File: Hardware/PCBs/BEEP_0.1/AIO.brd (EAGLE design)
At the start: 102 x 102 mm, 89 parts, among them U1 ATXMEGA64D3-AU, U2 TB6612FNG

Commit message: enhance robot case enhance main circuit
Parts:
- removed JP10: (no value), pinhead:1X08
- removed U$10, U$11, U$12, U$14, U$15, U$16, U$17, U$18, U$19, U$20, U$6, U$7, U$8, U$9: DMN2075U, BEEP:SOT95P240X112-3N
- added IC1, IC2: ULN2803ASOP18, BEEP:SOP18
- added JP12: Step_Down_Conn, pinhead:1X03
- added JP13: batt_conn, pinhead:1X02
- added LED11: (no value), led:CHIPLED_0603
- added R35, R36, R37, R38, R40, R41: 100R, rcl:R0402
- added R39: 47K, rcl:R0402
- added R42: (no value), rcl:R0402
- added S1, S2: (no value), switch-omron:B3F-31XX
- JP11: value (none) -> Color_Conn
- JP9: value (none) -> Motor_Conn; device pinhead:1X08 -> pinhead:1X04
- R34: value (none) -> 10K
- moved R34 132.4 mm to (40.6, 66.0)
- moved C5 81.2 mm to (14.0, 47.0)
- moved LED10 81.2 mm to (14.0, 55.9)
- moved LED9 81.2 mm to (19.1, 55.9)
- moved R28 81.2 mm to (24.1, 62.2)
- moved R29 81.2 mm to (24.1, 58.4)
- moved R30 81.2 mm to (24.1, 54.6)
- moved R33 81.2 mm to (14.0, 38.1)
- moved R31 81.2 mm to (14.0, 50.8)
- moved R32 81.2 mm to (14.0, 41.9)
- moved JP8 79.5 mm to (100.3, 0.00), turned to 225 degrees
- moved U$5 71.9 mm to (15.2, 47.0), turned to 0 degrees
- moved R5 49.9 mm to (97.8, 68.6)
- moved JP11 48.1 mm to (10.2, 41.9), turned to 90 degrees
- moved JP5 38.2 mm to (11.4, 3.81)
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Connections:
- removed net IR_DISTANCE_0: U$12.G
- removed net IR_DISTANCE_1: U$14.G
- removed net IR_DISTANCE_2: U$15.G
- removed net IR_DISTANCE_3: U$16.G
- removed net IR_DISTANCE_4: U$17.G
- removed net IR_DISTANCE_5: U$18.G
- removed net IR_DISTANCE_6: U$19.G
- removed net IR_DISTANCE_7: U$20.G
- removed net LEDA1: U$3.G
- removed net LEDA2: U$2.G
- removed net LEDA3: U$1.G
- removed net LEDK1: U$4.G
- removed net LEDK2: U$5.G
- removed net LEDK3: U$6.G
- removed net LEDK4: U$7.G
- removed net LEDK5: U$8.G
- removed net LEDK6: U$9.G
- removed net LEDK7: U$10.G
- removed net LEDK8: U$11.G
- removed net N$28: R14.1, U$18.S
- removed net N$31: R16.1, U$19.S
- removed net N$37: R18.1, U$20.S
- new net BATT_GND: JP13.2, U$5.S
- new net IR_LED1: IC2.1
- new net IR_LED2: IC2.2
- new net IR_LED3: IC2.3
- new net IR_LED4: IC2.4
- new net IR_LED5: IC2.5
- new net IR_LED6: IC2.6
- new net IR_LED7: IC2.7
- new net IR_LED8: IC2.8
- new net IR_PWM: R40.1
- new net LED1: IC1.1
- new net LED2: IC1.2
- new net LED3: IC1.3
- new net LED4: IC1.4
- new net LED5: IC1.5
- new net LED6: IC1.6
- new net LED7: IC1.7
- new net LED8: IC1.8
- new net LED_A1: R35.1
- new net LED_A2: R36.1
- new net LED_A3: R37.1
- new net N$38: R35.2, U$3.G
- new net N$39: R36.2, U$2.G
- new net N$40: R37.2, U$1.G
- new net N$41: U$26.5V@1, U$26.5V@2, U$4.S
- new net N$42: R38.2, R39.1, U$4.G
- new net N$43: IC2.15, JP4.3
- new net N$44: IC2.18, JP1.3
- new net N$45: IC2.17, JP2.3
- new net N$46: IC2.16, JP3.3
- new net N$47: IC2.13, JP6.3
- new net N$48: IC2.14, JP5.3
- new net N$49: IC2.12, JP7.3
- new net RPI_IKILL: R38.1
- net +3V3: no longer JP10.7
- net +5V: now also JP12.3, R39.2, U$13.D, U$4.D; no longer U$12.D, U$14.D, U$15.D, U$16.D, U$17.D, U$18.D, U$19.D, U$20.D, U$26.5V@1, U$26.5V@2
- net +7V: now also JP12.1, JP13.1, LED11.A, R41.1; no longer JP10.8
- net GND: now also IC1.9, IC2.9, JP12.2, R42.2, S1.2, S2.2, U$5.D; no longer JP10.1, JP10.6, JP9.8, U$10.S, U$11.S, U$13.S, U$4.S, U$5.S, U$6.S, U$7.S, U$8.S, U$9.S
- net IR_LED_PWM: now also R40.2
- net MOTOR_A_IN1: no longer JP9.3
- net MOTOR_A_IN2: no longer JP9.2
- net MOTOR_A_OUT1: now also JP9.4; no longer JP10.5
- net MOTOR_A_OUT2: now also JP9.3; no longer JP10.4
- net MOTOR_A_PWM: no longer JP9.1
- net MOTOR_B_IN1: no longer JP9.5
- net MOTOR_B_IN2: no longer JP9.6
- net MOTOR_B_OUT1: now also JP9.1; no longer JP10.2
- net MOTOR_B_OUT2: now also JP9.2; no longer JP10.3
- net MOTOR_B_PWM: no longer JP9.7
- net MOTOR_STBY: no longer JP9.4
- net N$10: now also IC1.15; no longer U$7.D
- net N$12: now also R10.1, R12.1, R14.1, R16.1, R18.1, R4.1, R8.1, U$13.S; no longer U$14.S
- net N$13: now also IC2.11; no longer JP1.3, JP2.3, JP3.3, JP4.3, JP5.3, JP6.3, JP7.3, U$13.D
- net N$14: now also IC1.14; no longer U$8.D
- net N$15: now also IC1.13; no longer U$9.D
- net N$16: now also IC1.12; no longer U$10.D
- net N$17: now also IC1.11; no longer U$11.D
- net N$19: now also LED11.C, R42.1; no longer R8.1, U$15.S
- net N$22: now also S1.1, U$26.GPIO_23; no longer R10.1, U$16.S
- net N$25: now also S2.1, U$26.GPIO_22; no longer R12.1, U$17.S
- net N$4: now also IC1.17; no longer U$5.D
- net N$6: now also IC1.18; no longer U$4.D
- net N$7: now also IC1.16; no longer U$6.D
- net N$8: now also R41.2, U$5.G; no longer R4.1, U$12.S
- net SCL: now also U$26.GPIO_1
- net SDA: now also U$26.GPIO_0
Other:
- board size 102 x 102 mm -> 105 x 80 mm

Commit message: minor enhancement of robot case enhancements of RPi Footprint enhance main pcb add pcb space drawing
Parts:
- moved IC2 18.0 mm to (50.8, 34.3), turned to 90 degrees
- moved U1 11.5 mm to (67.3, 39.4)
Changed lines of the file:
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@@
 </autorouter>
 <elements>
-<element name="U1" library="atmel-xmega" package="TQFP-64A-64" value="ATXMEGA64D3-AU" x="78.74" y="38.1"/>
+<element name="U1" library="atmel-xmega" package="TQFP-64A-64" value="ATXMEGA64D3-AU" x="67.31" y="39.37"/>
 <element name="LED1" library="BEEP" package="5050LED" value="F503605050" x="25.4" y="72.39"/>
 <element name="LED2" library="BEEP" package="5050LED" value="F503605050" x="74.93" y="8.89" rot="R180"/>
@@
 <element name="R38" library="rcl" package="R0402" value="100R" x="40.64" y="34.29"/>
 <element name="R39" library="rcl" package="R0402" value="47K" x="40.64" y="30.48"/>
-<element name="IC2" library="BEEP" package="SOP18" value="ULN2803ASOP18" x="63.5" y="21.59"/>
+<element name="IC2" library="BEEP" package="SOP18" value="ULN2803ASOP18" x="50.8" y="34.29" rot="R90"/>
 <element name="R40" library="rcl" package="R0402" value="100R" x="12.7" y="55.88"/>
 <element name="U$5" library="BEEP" package="SOT95P240X112-3N" value="DMN2075U" x="15.24" y="46.99"/>
@@
 <wire x1="56.205" y1="55.726" x2="57.505" y2="48.414" width="0" layer="19" extent="1-1"/>
 <wire x1="13.32" y1="67.31" x2="24.78" y2="58.42" width="0" layer="19" extent="1-1"/>
-<wire x1="75.94" y1="45.9" x2="58.155" y2="48.414" width="0" layer="19" extent="1-1"/>
-<wire x1="82.34" y1="45.9" x2="75.94" y2="45.9" width="0" layer="19" extent="1-1"/>
-<wire x1="83.17" y1="41.91" x2="82.34" y2="45.9" width="0" layer="19" extent="1-1"/>
-<wire x1="86.54" y1="40.9" x2="83.17" y2="41.91" width="0" layer="19" extent="1-1"/>
-<wire x1="86.54" y1="32.9" x2="86.54" y2="40.9" width="0" layer="19" extent="1-1"/>
-<wire x1="78.34" y1="30.3" x2="86.54" y2="32.9" width="0" layer="19" extent="1-1"/>
-<wire x1="73.66" y1="26.065" x2="78.34" y2="30.3" width="0" layer="19" extent="1-1"/>
-<wire x1="70.94" y1="33.7" x2="73.66" y2="26.065" width="0" layer="19" extent="1-1"/>
-<wire x1="68.58" y1="17.115" x2="73.66" y2="26.065" width="0" layer="19" extent="1-1"/>
-<wire x1="66.69" y1="11.43" x2="68.58" y2="17.115" width="0" layer="19" extent="1-1"/>
+<wire x1="64.51" y1="47.17" x2="58.155" y2="48.414" width="0" layer="19" extent="1-1"/>
+<wire x1="70.91" y1="47.17" x2="64.51" y2="47.17" width="0" layer="19" extent="1-1"/>
+<wire x1="83.17" y1="41.91" x2="70.91" y2="47.17" width="0" layer="19" extent="1-1"/>
+<wire x1="75.11" y1="42.17" x2="83.17" y2="41.91" width="0" layer="19" extent="1-1"/>
+<wire x1="75.11" y1="34.17" x2="75.11" y2="42.17" width="0" layer="19" extent="1-1"/>
+<wire x1="66.91" y1="31.57" x2="75.11" y2="34.17" width="0" layer="19" extent="1-1"/>
+<wire x1="73.66" y1="26.065" x2="66.91" y2="31.57" width="0" layer="19" extent="1-1"/>
+<wire x1="59.51" y1="34.97" x2="73.66" y2="26.065" width="0" layer="19" extent="1-1"/>
+<wire x1="55.275" y1="39.37" x2="73.66" y2="26.065" width="0" layer="19" extent="1-1"/>
+<wire x1="66.69" y1="11.43" x2="55.275" y2="39.37" width="0" layer="19" extent="1-1"/>
 <wire x1="63.5" y1="5.89" x2="66.69" y2="11.43" width="0" layer="19" extent="1-1"/>
-<wire x1="79.36" y1="11.43" x2="68.58" y2="17.115" width="0" layer="19" extent="1-1"/>
-<wire x1="99.0346" y1="44.1706" x2="86.54" y2="40.9" width="0" layer="19" extent="1-1"/>
+<wire x1="79.36" y1="11.43" x2="55.275" y2="39.37" width="0" layer="19" extent="1-1"/>
+<wire x1="99.0346" y1="44.1706" x2="75.11" y2="42.17" width="0" layer="19" extent="1-1"/>
 </signal>
 <signal name="N$10">
@@
 <contactref element="JP6" pad="2"/>
 <wire x1="96.52" y1="60.96" x2="86.36" y2="73.66" width="0" layer="19" extent="1-1"/>
-<wire x1="81.54" y1="45.9" x2="96.52" y2="60.96" width="0" layer="19" extent="1-1"/>
-<wire x1="86.54" y1="41.7" x2="81.54" y2="45.9" width="0" layer="19" extent="1-1"/>
-<wire x1="86.54" y1="33.7" x2="86.54" y2="41.7" width="0" layer="19" extent="1-1"/>
-<wire x1="79.14" y1="30.3" x2="86.54" y2="33.7" width="0" layer="19" extent="1-1"/>
-<wire x1="70.94" y1="32.9" x2="79.14" y2="30.3" width="0" layer="19" extent="1-1"/>
-<wire x1="98.533946875" y1="23.9121" x2="86.54" y2="33.7" width="0" layer="19" extent="1-1"/>
+<wire x1="70.11" y1="47.17" x2="96.52" y2="60.96" width="0" layer="19" extent="1-1"/>
+<wire x1="75.11" y1="42.97" x2="70.11" y2="47.17" width="0" layer="19" extent="1-1"/>
+<wire x1="75.11" y1="34.97" x2="75.11" y2="42.97" width="0" layer="19" extent="1-1"/>
+<wire x1="67.71" y1="31.57" x2="75.11" y2="34.97" width="0" layer="19" extent="1-1"/>
+<wire x1="59.51" y1="34.17" x2="67.71" y2="31.57" width="0" layer="19" extent="1-1"/>
+<wire x1="98.533946875" y1="23.9121" x2="75.11" y2="34.97" width="0" layer="19" extent="1-1"/>
 <wire x1="98.533946875" y1="3.5921" x2="98.533946875" y2="23.9121" width="0" layer="19" extent="1-1"/>
 <wire x1="60.96" y1="77.93" x2="86.36" y2="73.66" width="0" layer="19" extent="16-16"/>
@@
 <contactref element="JP8" pad="3"/>
 <contactref element="IC2" pad="11"/>
-<wire x1="67.31" y1="26.09" x2="94.94184375" y2="3.5921" width="0" layer="19" extent="1-1"/>
+<wire x1="46.3" y1="38.1" x2="94.94184375" y2="3.5921" width="0" layer="19" extent="1-1"/>
 </signal>
 <signal name="IR_LED_PWM">
@@
 <contactref element="SV1" pad="1"/>
 <contactref element="U1" pad="56"/>
-<wire x1="49.53" y1="74.93" x2="79.14" y2="45.9" width="0" layer="19" extent="1-1"/>
+<wire x1="49.53" y1="74.93" x2="67.71" y2="47.17" width="0" layer="19" extent="1-1"/>
 </signal>
 <signal name="PDI_CLK">
@@
 <contactref element="U1" pad="57"/>
 <contactref element="R34" pad="2"/>
-<wire x1="41.29" y1="66.04" x2="78.34" y2="45.9" width="0" layer="19" extent="1-1"/>
+<wire x1="41.29" y1="66.04" x2="66.91" y2="47.17" width="0" layer="19" extent="1-1"/>
 </signal>
 <signal name="RPI_TX">
@@
 <contactref element="JP4" pad="3"/>
 <contactref element="IC2" pad="15"/>
-<wire x1="2.3221" y1="25.708153125" x2="62.23" y2="26.09" width="0" layer="19" extent="1-1"/>
+<wire x1="2.3221" y1="25.708153125" x2="46.3" y2="33.02" width="0" layer="19" extent="1-1"/>
 </signal>
 <signal name="N$44">
 <contactref element="JP1" pad="3"/>
 <contactref element="IC2" pad="18"/>
-<wire x1="58.42" y1="26.09" x2="88.9" y2="71.12" width="0" layer="19" extent="1-1"/>
+<wire x1="46.3" y1="29.21" x2="88.9" y2="71.12" width="0" layer="19" extent="1-1"/>
 </signal>
 <signal name="N$45">
 <contactref element="JP2" pad="3"/>
 <contactref element="IC2" pad="17"/>
-<wire x1="7.62" y1="60.96" x2="59.69" y2="26.09" width="0" layer="19" extent="1-1"/>
+<wire x1="7.62" y1="60.96" x2="46.3" y2="30.48" width="0" layer="19" extent="1-1"/>
 </signal>
 <signal name="N$46">
 <contactref element="JP3" pad="3"/>
 <contactref element="IC2" pad="16"/>
-<wire x1="16.881971875" y1="70.221971875" x2="60.96" y2="26.09" width="0" layer="19" extent="1-1"/>
+<wire x1="16.881971875" y1="70.221971875" x2="46.3" y2="31.75" width="0" layer="19" extent="1-1"/>
 </signal>
 <signal name="N$48">
 <contactref element="JP5" pad="3"/>
 <contactref element="IC2" pad="14"/>
-<wire x1="10.16" y1="10.16" x2="63.5" y2="26.09" width="0" layer="19" extent="1-1"/>
+<wire x1="10.16" y1="10.16" x2="46.3" y2="34.29" width="0" layer="19" extent="1-1"/>
 </signal>
 <signal name="N$47">
 <contactref element="JP6" pad="3"/>
 <contactref element="IC2" pad="13"/>
-<wire x1="64.77" y1="26.09" x2="94.94184375" y2="23.9121" width="0" layer="19" extent="1-1"/>
+<wire x1="46.3" y1="35.56" x2="94.94184375" y2="23.9121" width="0" layer="19" extent="1-1"/>
 </signal>
 <signal name="N$49">
 <contactref element="JP7" pad="3"/>
 <contactref element="IC2" pad="12"/>
-<wire x1="66.04" y1="26.09" x2="93.98" y2="58.42" width="0" layer="19" extent="1-1"/>
+<wire x1="46.3" y1="36.83" x2="93.98" y2="58.42" width="0" layer="19" extent="1-1"/>
 </signal>
 <signal name="N$12">

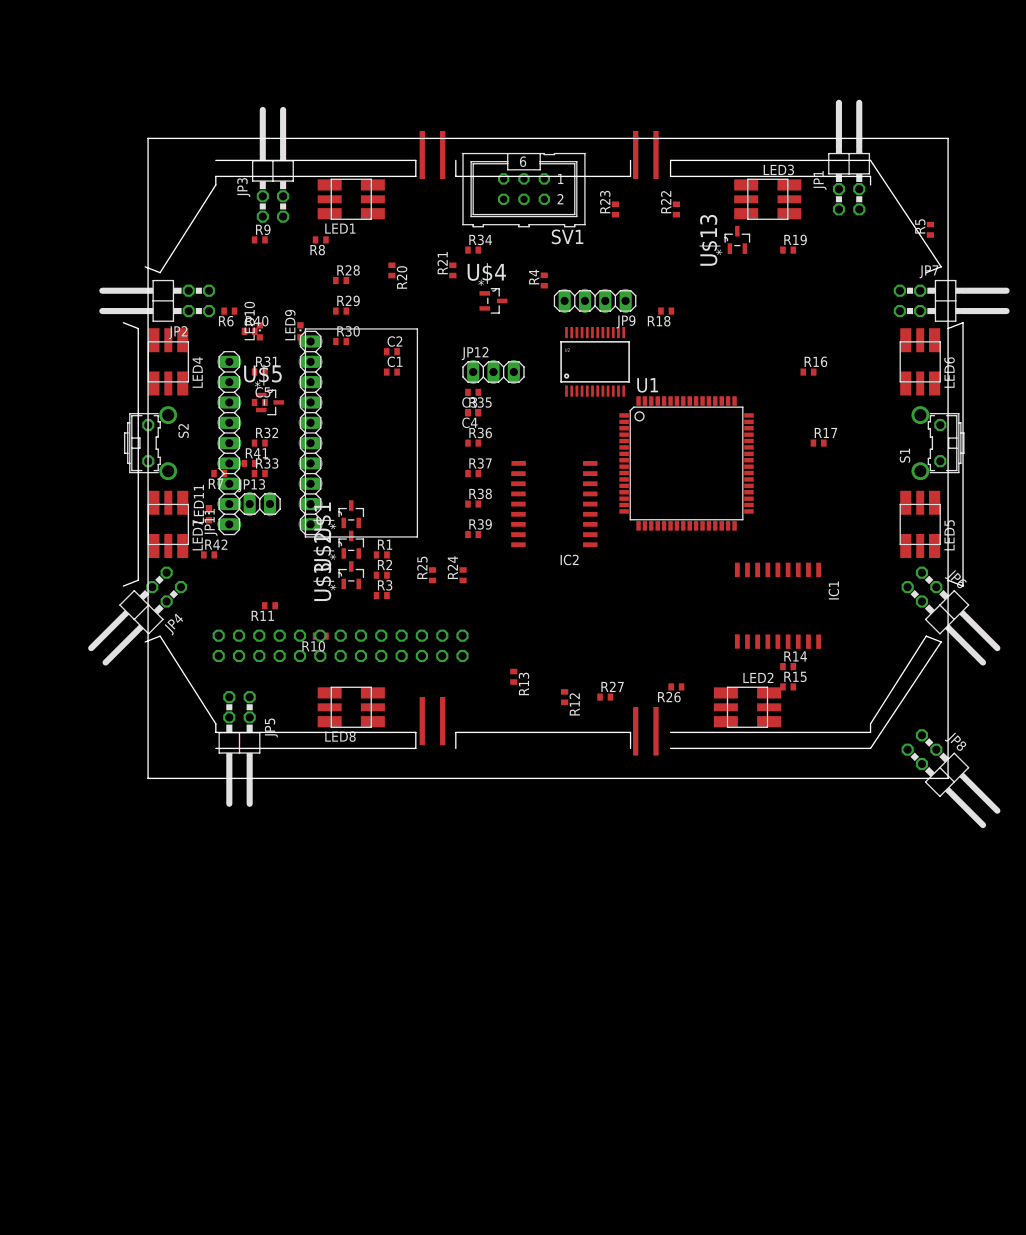
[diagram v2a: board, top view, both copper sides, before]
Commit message: add robot pcb space to eagle pcb enhance circuit
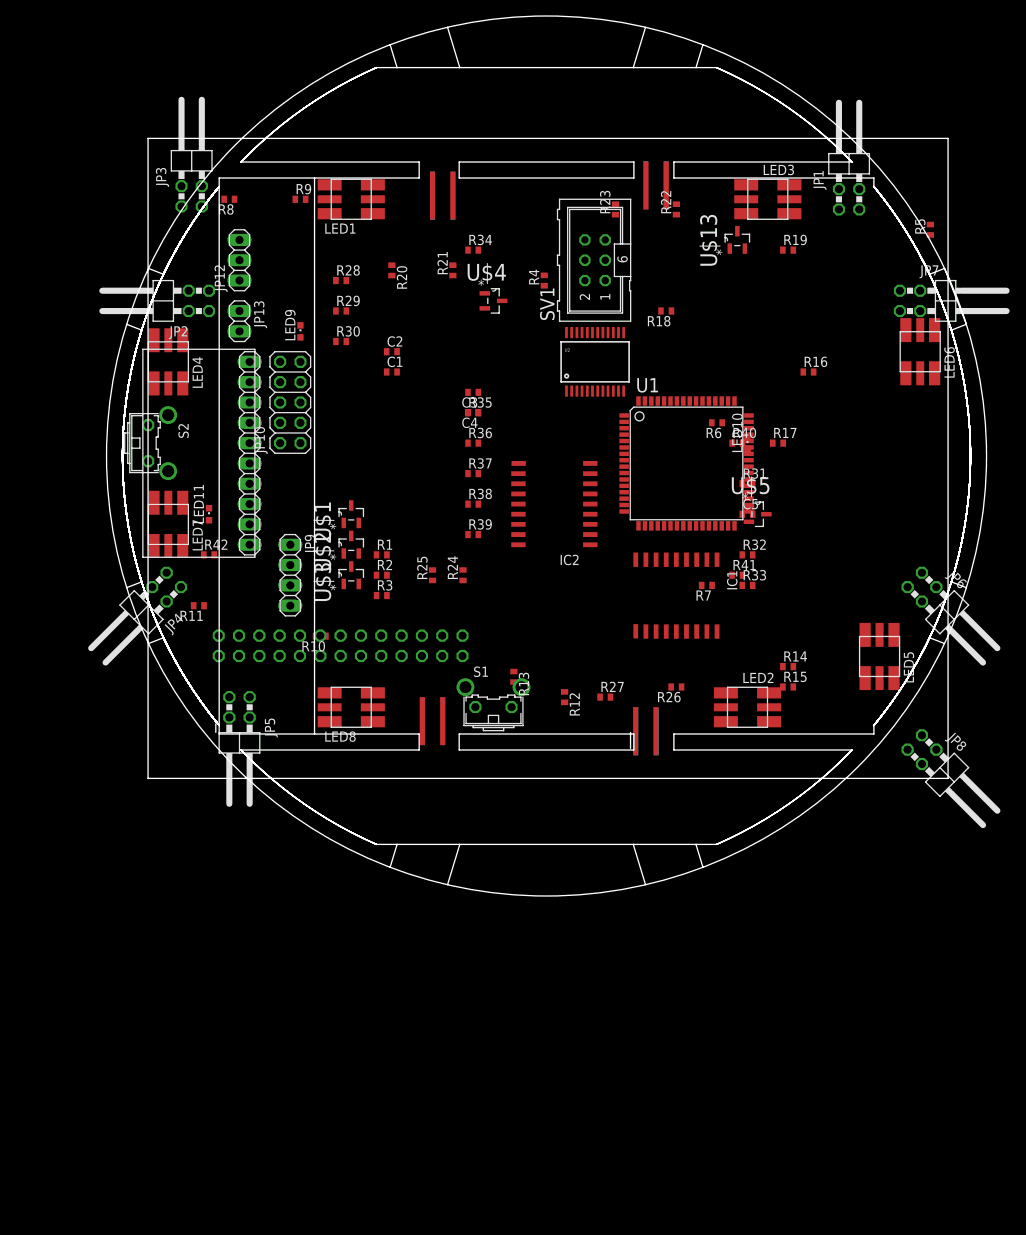
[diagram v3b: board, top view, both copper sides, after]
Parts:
- removed JP11: Color_Conn, pinhead:1X09
- added JP10: (no value), pinhead:2X05
- moved S1 63.2 mm to (43.2, 10.2), turned to 0 degrees
- moved C5 62.5 mm to (74.9, 33.0)
- moved LED10 62.5 mm to (74.9, 41.9)
- moved R31 62.5 mm to (74.9, 36.8)
- moved R32 62.5 mm to (74.9, 27.9)
- moved R33 62.5 mm to (74.9, 24.1)
- moved R6 62.5 mm to (71.1, 44.5)
- moved U$5 62.5 mm to (76.2, 33.0)
- moved R40 62.5 mm to (73.7, 41.9)
- moved R41 62.5 mm to (73.7, 25.4)
- moved R7 62.5 mm to (69.8, 24.1)
- moved JP9 51.3 mm to (17.8, 25.4), turned to 270 degrees
- moved JP12 34.7 mm to (11.4, 64.8), turned to 90 degrees
- moved JP13 23.0 mm to (11.4, 57.1), turned to 270 degrees
- moved U$25 20.5 mm to (6.35, 40.6), turned to 90 degrees
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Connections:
- net +3V3: now also JP10.3; no longer JP11.2
- net +5V: now also JP10.1; no longer JP11.1
- net COLOR_DIODE_1: now also JP10.6; no longer JP11.7
- net COLOR_DIODE_2: now also JP10.4; no longer JP11.8
- net COLOR_FREQ_OUT: now also JP10.7; no longer JP11.9
- net COLOR_SENSOR_1: now also JP10.2; no longer JP11.4
- net COLOR_SENSOR_2: now also JP10.10; no longer JP11.5
- net COLOR_SENSOR_3: now also JP10.8; no longer JP11.6
- net GND: now also JP10.5; no longer JP11.3
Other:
- board size 105 x 80 mm -> 110 x 110 mm
